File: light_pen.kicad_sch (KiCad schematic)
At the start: 6 parts, among them J8 Conn_01x06_Male, U14 74LS05, U3 74F04

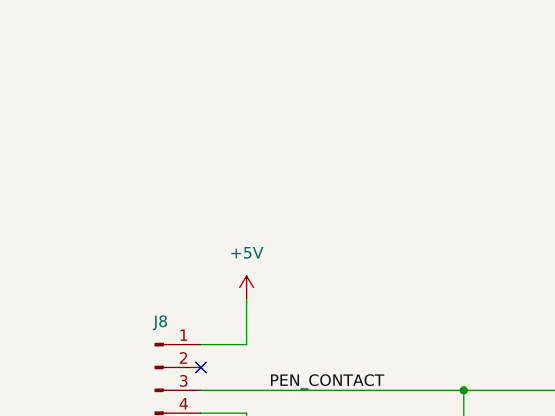
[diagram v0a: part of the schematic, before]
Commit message: Improved signal naming
clearer naming of some signals for better readability
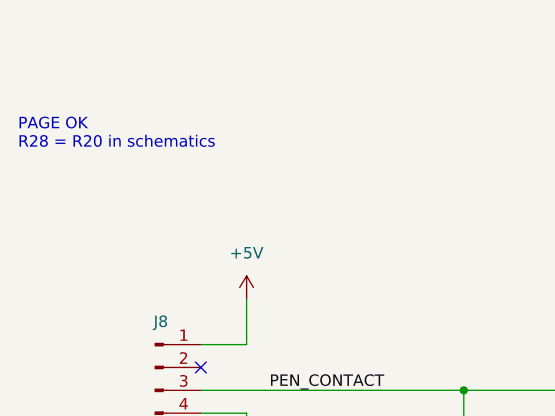
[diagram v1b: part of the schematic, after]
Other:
- note added: "PAGE OK R28 = R20 in schematics"
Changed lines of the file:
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@@
     (effects (font (size 5 5)) (justify left bottom))
+  )
+  (text "PAGE OK\nR28 = R20 in schematics" (at 59.69 43.18 0)
+    (effects (font (size 1.27 1.27)) (justify left bottom))
   )
   (label "PEN_CONTACT" (at 87.63 69.85 0) (fields_autoplaced)
